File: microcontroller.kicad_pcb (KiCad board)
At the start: 2 copper layers, 0 parts

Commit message: Finished schematic and PCB routing. Just need to touch up silkscreen.
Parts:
- added C1: 100nF, Capacitor_SMD:C_1206_3216Metric_Pad1.33x1.80mm_HandSolder, F.Cu at (148.0, 120.0)
- added F1: 0031.7701.11, FUSE_0031.7701.11_SCH:FUSE_0031.7701.11_SCH, F.Cu at (153.0, 68.5)
- added J1: Conn_01x02, Connector_JST:JST_EH_B2B-EH-A_1x02_P2.50mm_Vertical, F.Cu at (180.0, 60.0)
- added J2: SWD, Connector_PinHeader_2.54mm:PinHeader_1x03_P2.54mm_Vertical, F.Cu at (162.5, 70.0)
- added J3: PORT A, Connector_PinHeader_2.54mm:PinHeader_1x11_P2.54mm_Vertical, F.Cu at (182.0, 77.2)
- added J4: Conn_01x06, Connector_PinHeader_2.54mm:PinHeader_1x06_P2.54mm_Vertical, F.Cu at (148.5, 88.3)
- added J5: SPI 0, Connector_JST:JST_EH_B4B-EH-A_1x04_P2.50mm_Vertical, F.Cu at (158.5, 60.0)
- added J6: I2C 1, Connector_JST:JST_EH_B2B-EH-A_1x02_P2.50mm_Vertical, F.Cu at (169.0, 60.0)
- added J7: UART 1, Connector_JST:JST_EH_B2B-EH-A_1x02_P2.50mm_Vertical, F.Cu at (181.5, 69.5)
- added LED1: HSMS-C150, HSMS_C150:LED3_HSMx-C110_AVA, F.Cu at (182.0, 118.5)
- added R1: 330, Resistor_SMD:R_1206_3216Metric_Pad1.30x1.75mm_HandSolder, F.Cu at (182.0, 124.5)
- added U1: Pico, MCU_RaspberryPi_and_Boards:RPi_Pico_SMD_TH, F.Cu at (165.0, 99.5)
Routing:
- net GND: track 0.00 -> 178.8 mm
- net VCC: track 0.00 -> 63.3 mm
- net I2C1_SCL: track 0.00 -> 61.4 mm
- net UART1_TX: track 0.00 -> 60.3 mm
- net I2C1_SDA: track 0.00 -> 58.1 mm
- net UART1_RX: track 0.00 -> 48.9 mm
- net GPIO1: track 0.00 -> 42.6 mm
- net SPI0_TX: track 0.00 -> 32.4 mm
- net Net-(J1-Pin_1): track 0.00 -> 31.1 mm
- net SPI0_SCK: track 0.00 -> 28.5 mm
- net SPI0_CSn: track 0.00 -> 22.3 mm
- net SPI0_RX: track 0.00 -> 18.3 mm
- net GPIO28: track 0.00 -> 11.6 mm
- net GPIO27: track 0.00 -> 9.63 mm
- net GPIO26: track 0.00 -> 9.63 mm
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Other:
- board outline added: 40 x 70 mm

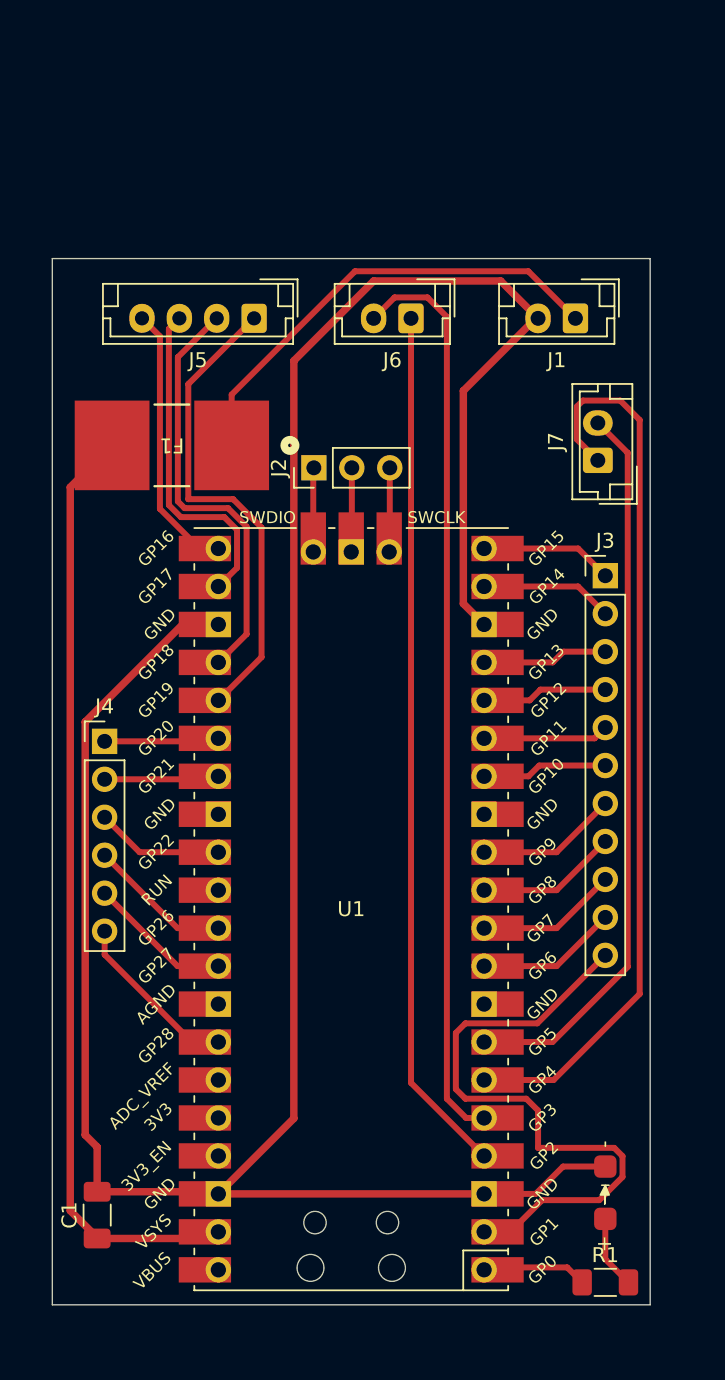
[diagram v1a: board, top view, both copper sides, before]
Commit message: Added ground planes.
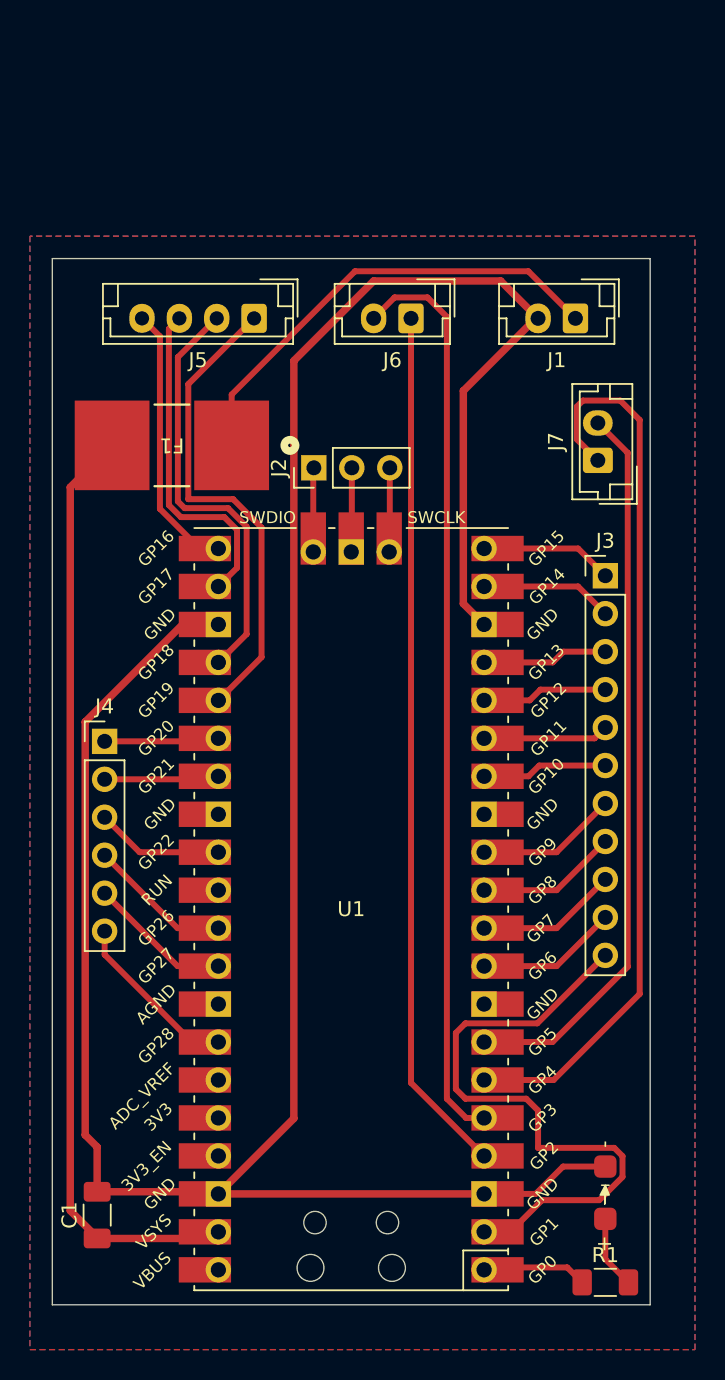
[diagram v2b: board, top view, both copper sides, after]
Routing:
- added copper zone on B.Cu, net GND
- added copper zone on F.Cu, net GND
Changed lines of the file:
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@@
 		(net 40)
 	)
+	(zone
+		(net 1)
+		(net_name "GND")
+		(layers "F&B.Cu")
+		(hatch edge 0.5)
+		(connect_pads
+			(clearance 0.5)
+		)
+		(min_thickness 0.25)
+		(filled_areas_thickness no)
+		(fill yes
+			(thermal_gap 0.5)
+			(thermal_bridge_width 0.5)
+			(island_removal_mode 1)
+			(island_area_min 10)
+		)
+		(polygon
+			(pts
+				(xy 143.5 129) (xy 188 129) (xy 188 54.5) (xy 143.5 54.5)
+			)
+		)
+	)
 )

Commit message: Added DB9 connector and always-on power LED.
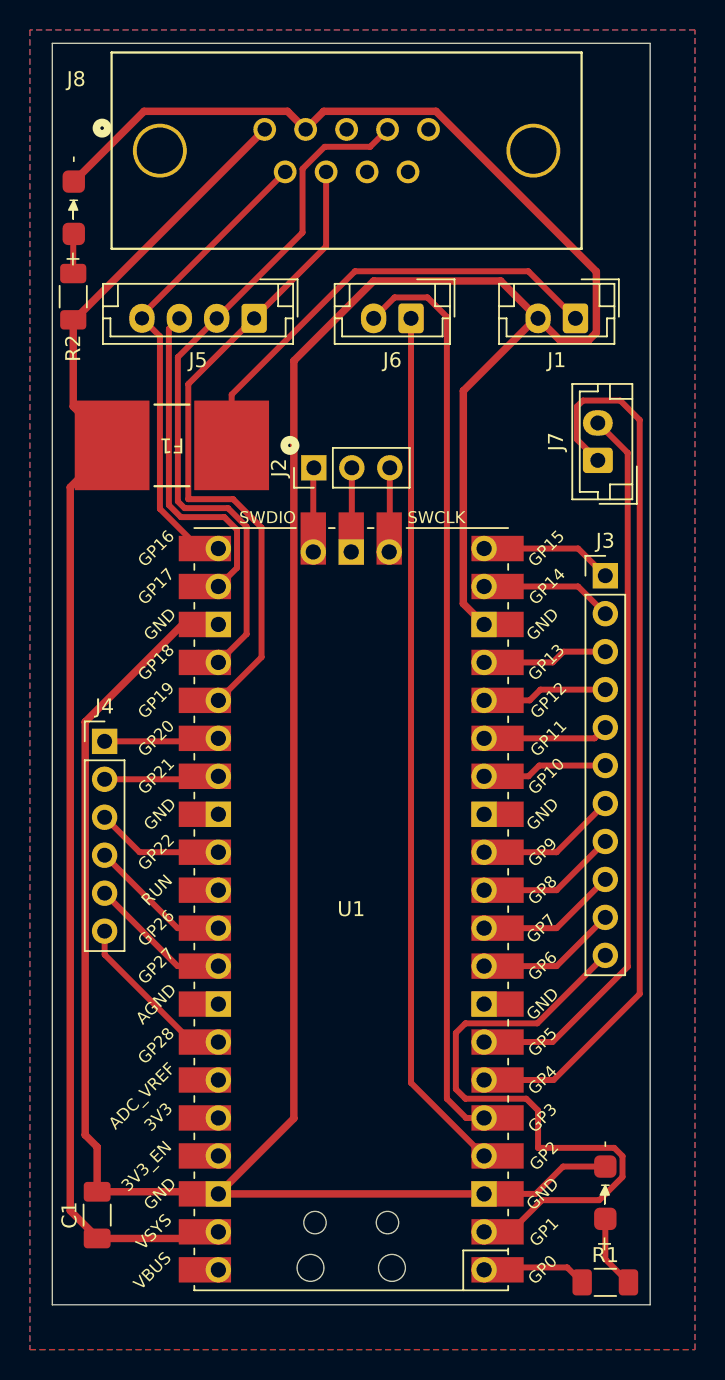
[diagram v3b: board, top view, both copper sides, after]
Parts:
- added J8: DE9_Plug, DE09P064TXLF:CONN_64TXLF_AMP, F.Cu at (159.2, 47.4)
- added LED2: HSMS-C150, HSMS_C150:LED3_HSMx-C110_AVA, F.Cu at (146.4, 52.6)
- added R2: 330, Resistor_SMD:R_1206_3216Metric_Pad1.30x1.75mm_HandSolder, F.Cu at (146.4, 58.5)
- J4: value Conn_01x06 -> PORT B
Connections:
- net POWER_LED renamed LED
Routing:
- net GND: track 178.8 -> 230.0 mm
- net VCC: track 63.3 -> 90.8 mm
- net SPI0_SCK: track 28.5 -> 47.6 mm
- net SPI0_RX: track 18.3 -> 32.0 mm
- net SPI0_TX: track 32.4 -> 44.2 mm
- net Net-(LED2-Pad1): track 0.00 -> 2.66 mm
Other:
- board size 40 x 70 mm -> 40 x 84.4 mm

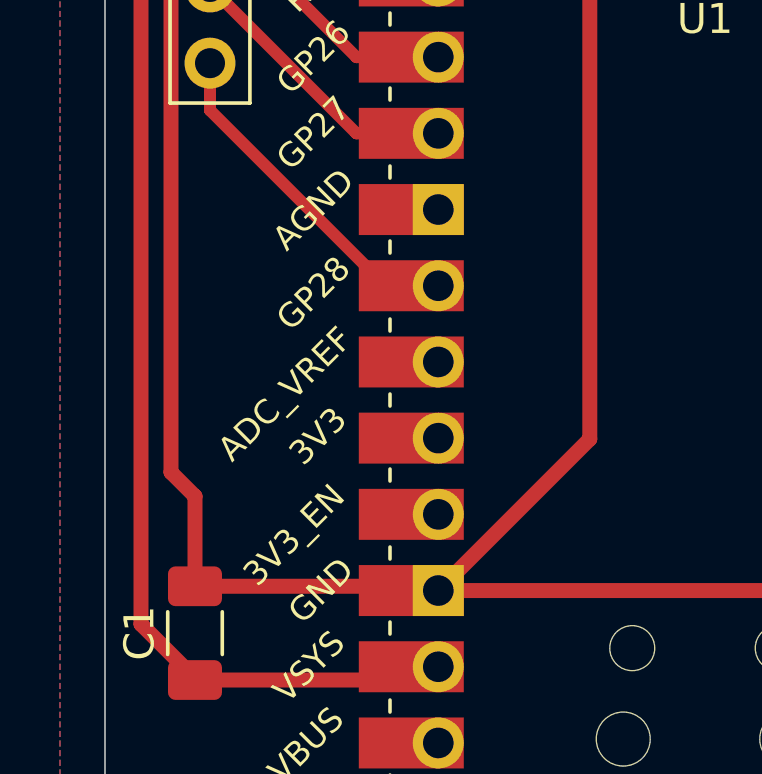
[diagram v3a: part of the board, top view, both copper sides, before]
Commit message: Added DB9 and 3v3 output pad.
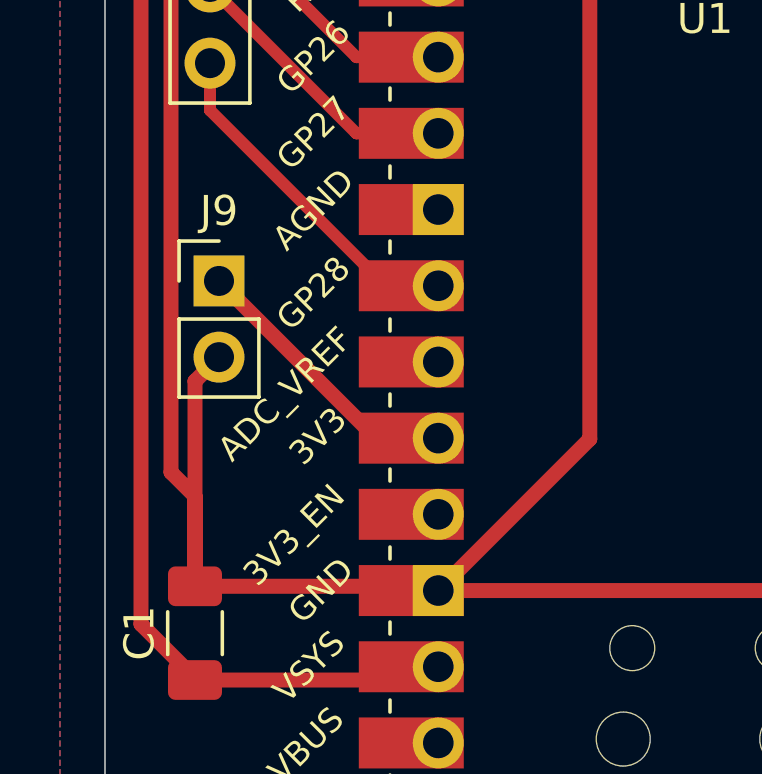
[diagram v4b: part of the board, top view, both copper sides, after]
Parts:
- added J9: Conn_01x02, Connector_PinHeader_2.54mm:PinHeader_1x02_P2.54mm_Vertical, F.Cu at (148.8, 108.3)
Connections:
- U1 pad 36: unconnected-(U1-3V3-Pad36) -> PICO_3V3
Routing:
- net PICO_3V3: track 0.00 -> 9.48 mm
- net GND: track 230.0 -> 237.9 mm

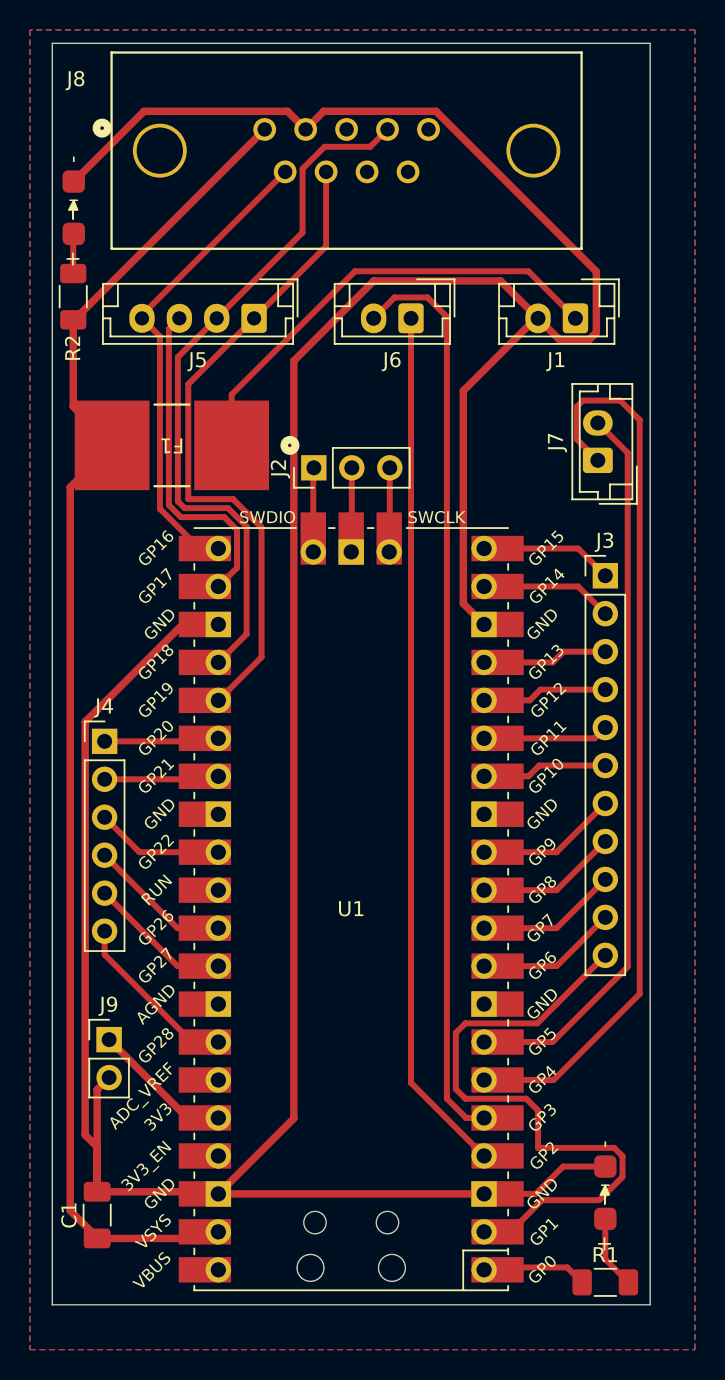
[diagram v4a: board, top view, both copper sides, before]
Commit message: Improved silkscreen (a lot) and added two more 3.3v breakout headers.
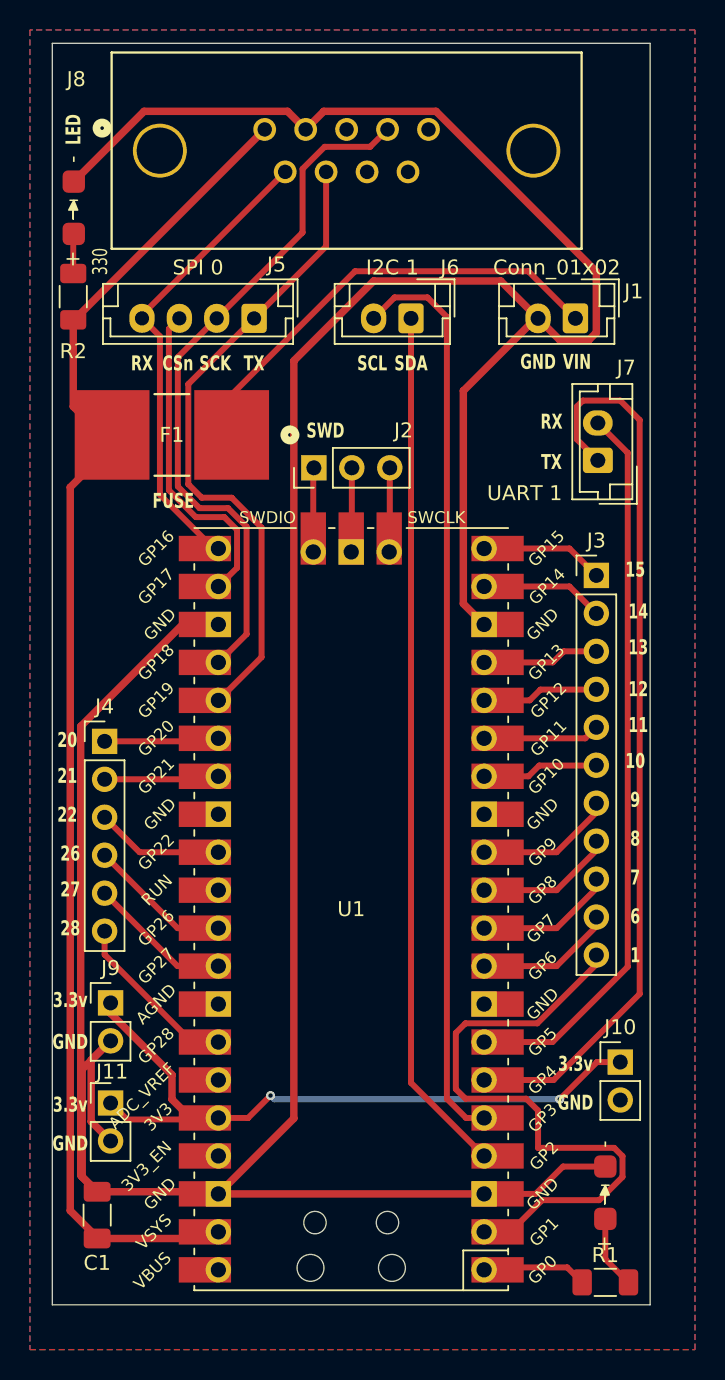
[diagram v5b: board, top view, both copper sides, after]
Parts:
- added J10: Conn_01x02, Connector_PinHeader_2.54mm:PinHeader_1x02_P2.54mm_Vertical, F.Cu at (183.0, 109.8)
- added J11: Conn_01x02, Connector_PinHeader_2.54mm:PinHeader_1x02_P2.54mm_Vertical, F.Cu at (148.9, 112.5)
- moved J9 2.46 mm to (148.9, 105.8)
- moved F1 0.70 mm to (153.0, 67.8)
- moved J3 0.60 mm to (181.4, 77.2)
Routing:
- net PICO_3V3: track 9.48 -> 48.1 mm, vias 0 -> 2
- net GND: track 237.9 -> 249.3 mm
- net Net-(J1-Pin_1): track 31.1 -> 30.4 mm
- net GPIO14: track 8.86 -> 8.26 mm
- net GPIO15: track 8.86 -> 8.26 mm
- net GPIO11: track 8.41 -> 7.82 mm
- net GPIO13: track 8.41 -> 7.82 mm
- net GPIO10: track 8.41 -> 7.82 mm
- net GPIO12: track 8.41 -> 7.82 mm
- net SPI0_TX: track 44.2 -> 43.6 mm
- net SPI0_CSn: track 22.3 -> 21.8 mm
- net SPI0_SCK: track 47.6 -> 47.1 mm
- net SPI0_RX: track 32.0 -> 31.5 mm
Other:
- board text added: "1"
- board text added: "10"
- board text added: "11"
- board text added: "12"
- board text added: "13"
- board text added: "14"
- board text added: "15"
- board text added: "20"
- board text added: "21"
- board text added: "22"
- board text added: "26"
- board text added: "27"
- board text added: "28"
- board text added: "3.3v"
- board text added: "6"
- board text added: "7"
- board text added: "8"
- board text added: "9"
- board text added: "CSn"
- board text added: "FUSE"
- board text added: "GND"
- board text added: "LED"
- board text added: "NC"
- board text added: "RX"
- board text added: "SCK"
- board text added: "SCL"
- board text added: "SDA"
- board text added: "SWD"
- board text added: "TX"
- board text added: "VCC"
- board text added: "VIN"
